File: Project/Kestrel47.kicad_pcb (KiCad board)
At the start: 2 copper layers, 247.6 x 76.2 mm, 97 parts, among them SW1 SW_Push, U1 ProMicro

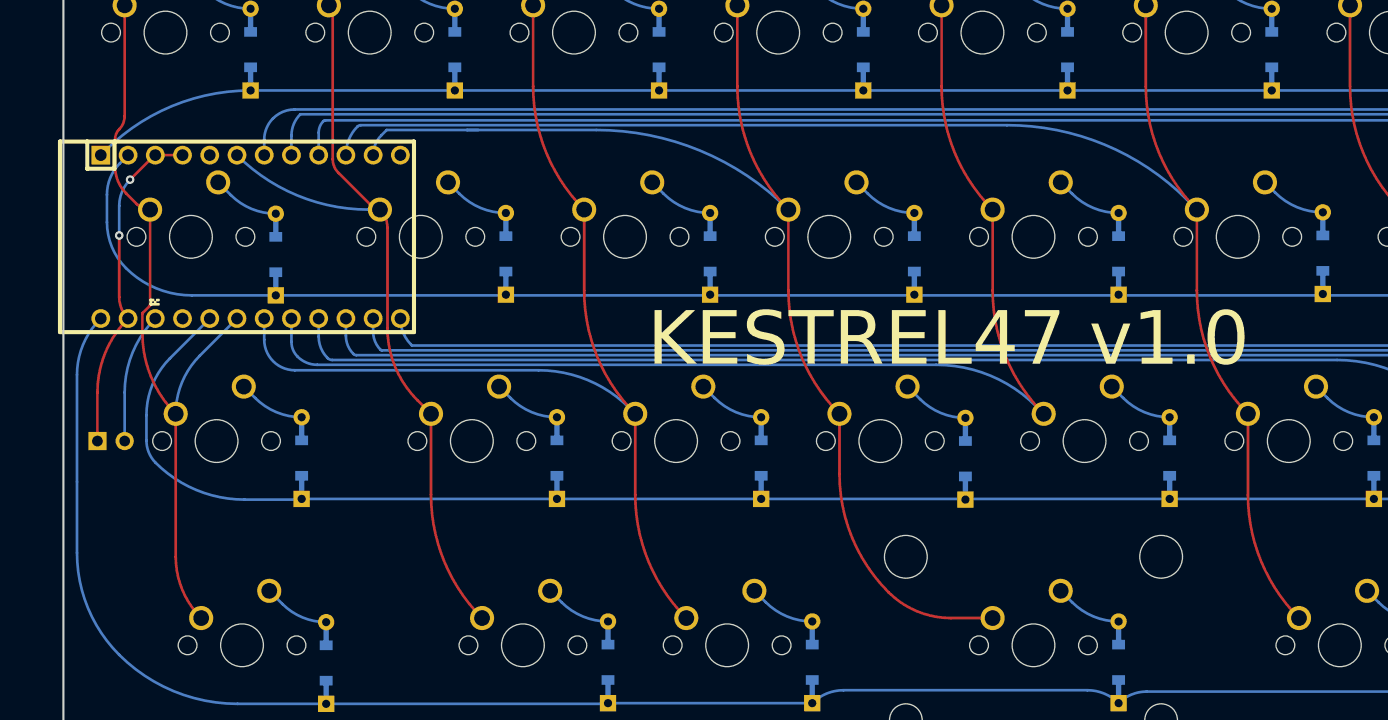
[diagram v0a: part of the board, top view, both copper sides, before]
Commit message: rerouting mistake, adding rgb and power button
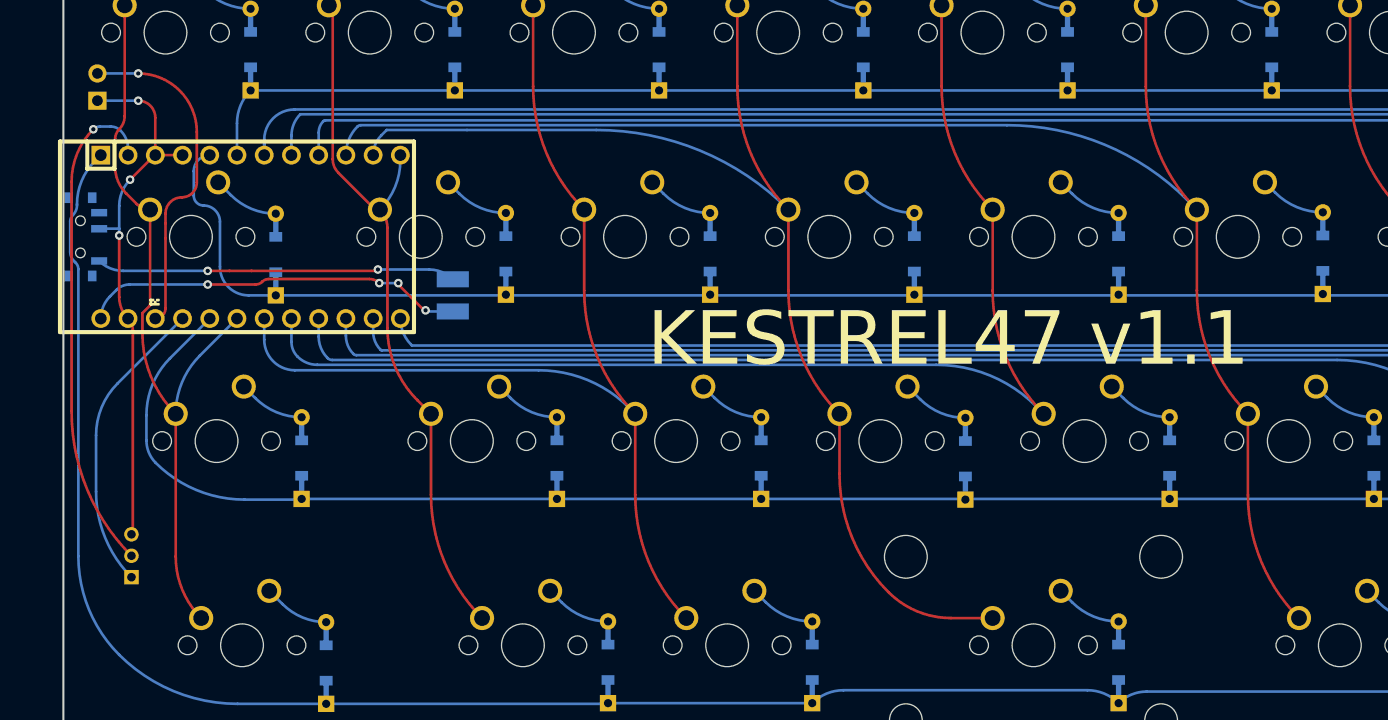
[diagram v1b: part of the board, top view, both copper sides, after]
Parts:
- added BT1: Battery_Cell, keeblib:cell_pads, B.Cu at (52.2, 49.9)
- added J1: Conn_01x03, Connector_PinSocket_2.00mm:PinSocket_1x03_P2.00mm_Vertical, B.Cu at (22.2, 76.2)
- added SW2: SW_SPDT, keeblib:switch_SSSS811101, B.Cu at (17.5, 44.5)
- moved SW1 31.8 mm to (19.1, 31.8), turned to 0 degrees
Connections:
- U1 pad 1: ROW0 ->  ROW3
- U1 pad 12: unconnected-(U1-Pad12) -> COL1
- U1 pad 2: ROW1 -> RGB
- U1 pad 24:  ROW3 -> RAW
- U1 pad 5: unconnected-(U1-Pad5) -> ROW1
- U1 pad 6: COL1 -> ROW0
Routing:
- net RGB: track 0.00 -> 46.8 mm, vias 0 -> 1
- net RAW: track 0.00 -> 36.2 mm, vias 0 -> 4
- net Net-(BT1-Pad2): track 0.00 -> 33.5 mm, vias 0 -> 2
- net VCC: track 0.00 -> 28.0 mm
- net GND: track 31.4 -> 51.0 mm, vias 2 -> 3
- net Net-(SW1-Pad2): track 12.1 -> 31.6 mm, vias 0 -> 1
- net  ROW3: track 274.6 -> 290.3 mm
- net ROW0: track 244.2 -> 235.0 mm
- net COL1: track 77.0 -> 68.0 mm
- net ROW1: track 245.3 -> 238.2 mm
- net COL3: track 111.7 -> 110.7 mm
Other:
- board text added: "KESTREL47 v1.1"
- board text added: "Power"
- board text added: "Rgb"
- board text removed: "KESTREL47 v1.0"
